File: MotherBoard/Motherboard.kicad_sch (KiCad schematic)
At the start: 31 parts, among them J1 22-28-4157, J2 X6521WV-2x15H-C60D30, Q1 NCE2302, SW1 FSM4JSMATR, SW2 FSM4JSMATR, U1 ESP32 S3, U2 Unidirectional 5.5V 6V SOT-14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, U4 LIS2MDLTR, U5 LIS3DHTR, U6 MAX7219M/TR, U7 C193852

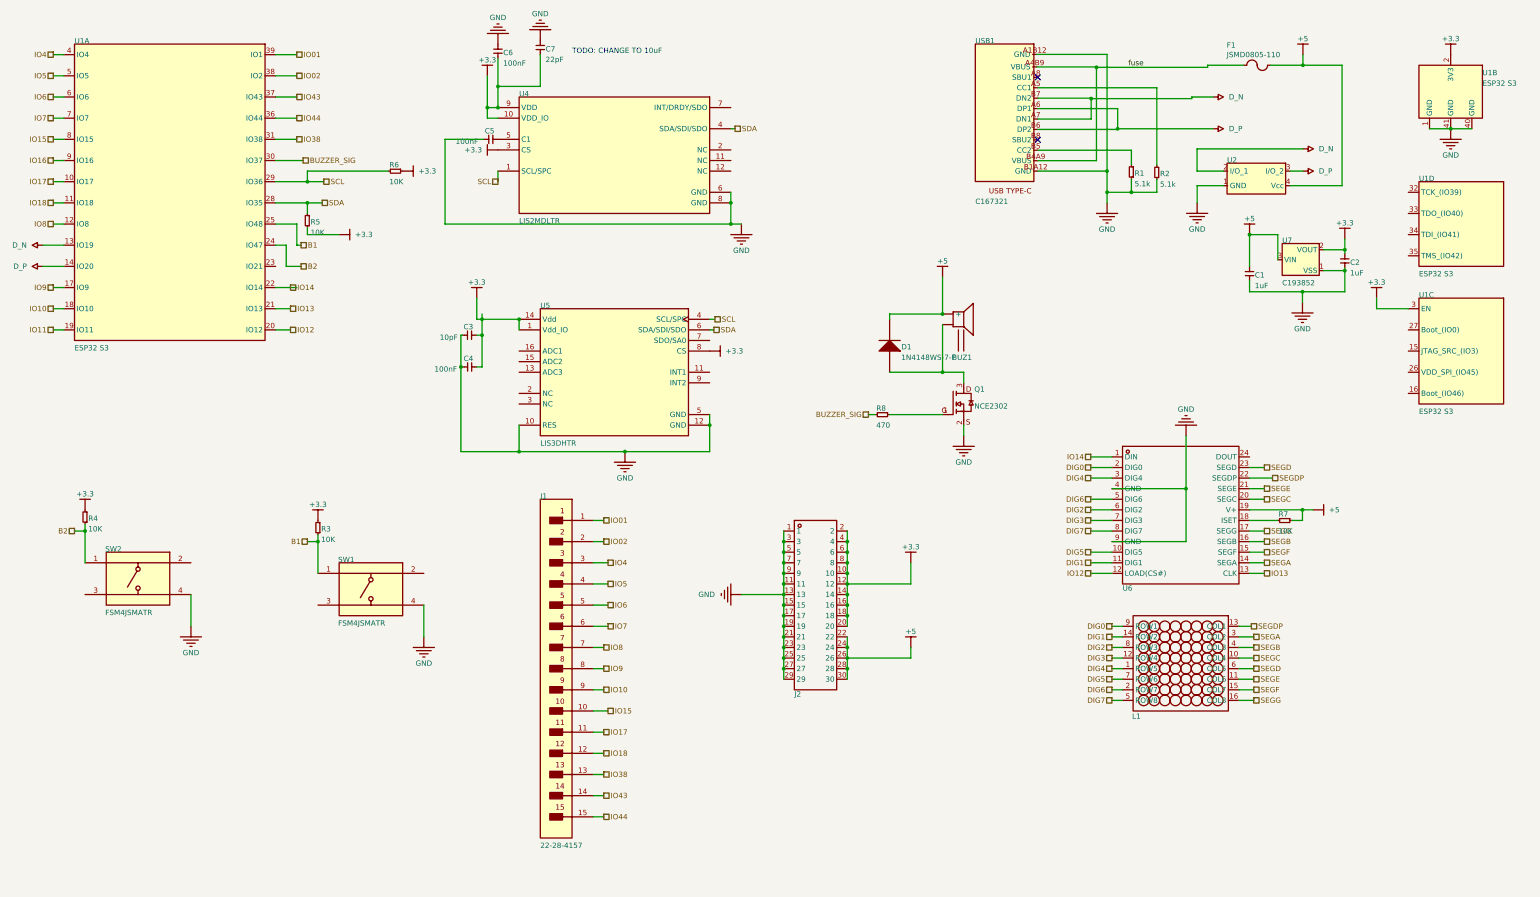
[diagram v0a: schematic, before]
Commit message: motherboard imported and corrected
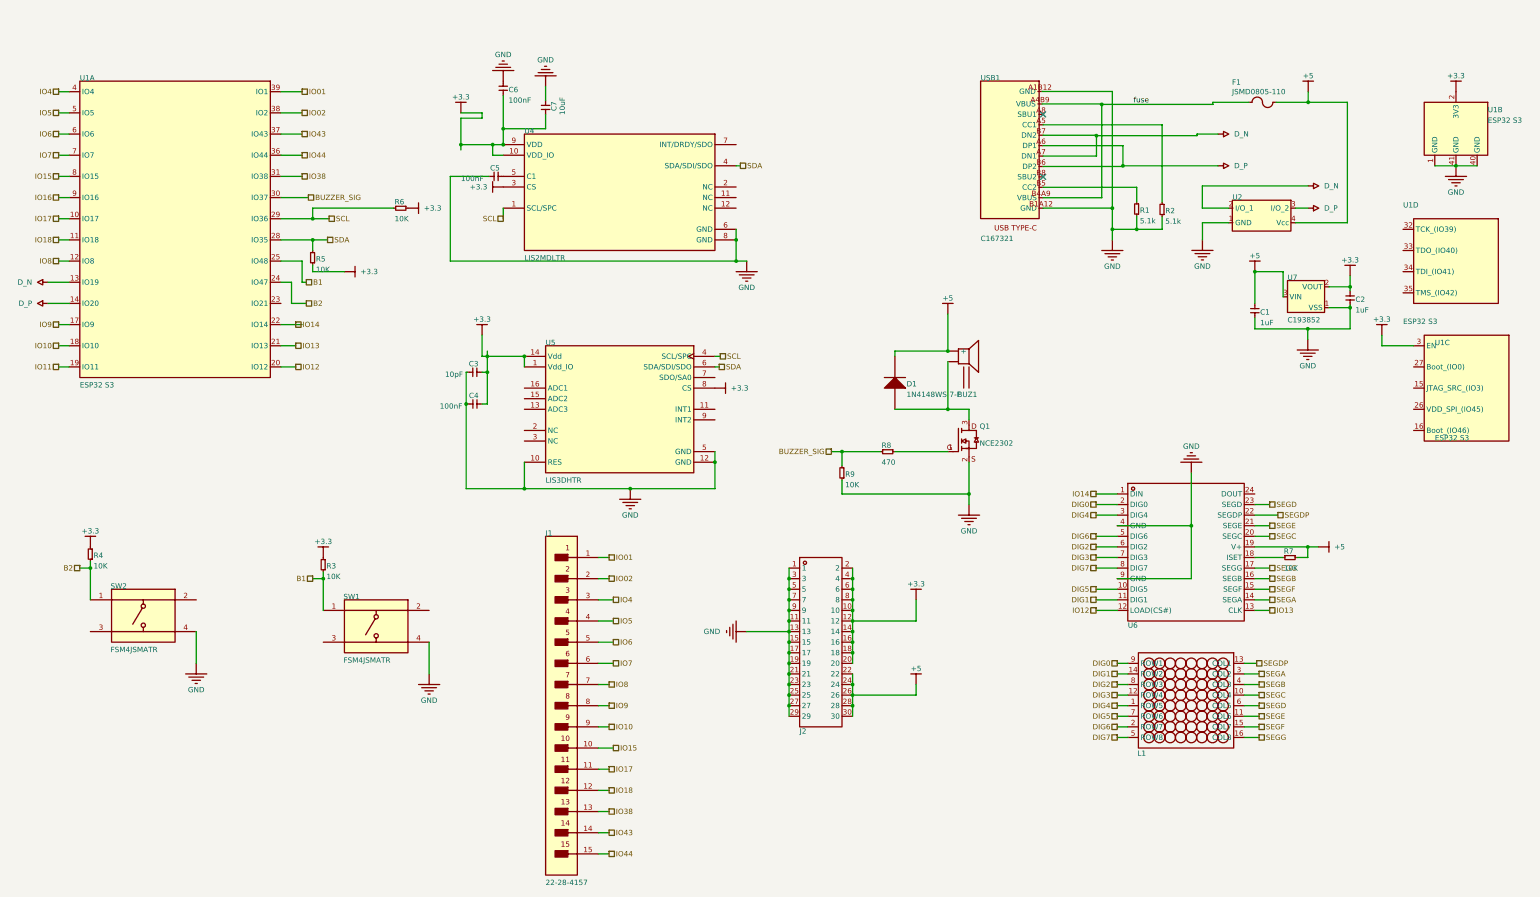
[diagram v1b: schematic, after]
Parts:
- removed C7: 22pF, 0402C, symbol Hub 2.0:root_1_TCC0402COG220K500AT_Hub 2.0.SchLib
- added C7: 10uF, FableFootPrintLibrary:0402C, symbol Hub 2.0:root_0_TCC0402COG100K500AT_Hub 2.0.SchLib
- added R9: 10K, FableFootPrintLibrary:0402R, symbol Hub 2.0:root_1_RC-02W103JT_Hub 2.0.SchLib
- BUZ1: footprint BUZ-SMD_4P-L8.5-W8.5-P8.50-BR -> FableFootPrintLibrary:BUZ-SMD_4P-L8.5-W8.5-P8.50-BR; SUPPLIER 1 (none) -> LCSC
- C1, C2: footprint 0402C -> FableFootPrintLibrary:0402C; SUPPLIER (none) -> LCSC; SUPPLIER PART (none) -> C60474; SUPPLIER PART NUMBER 1 C107372 -> C60474
- C3: footprint 0402C -> FableFootPrintLibrary:0402C; SUPPLIER (none) -> LCSC; SUPPLIER PART (none) -> C713505
- C4, C5, C6: footprint 0402C -> FableFootPrintLibrary:0402C; SUPPLIER (none) -> LCSC; SUPPLIER PART (none) -> C60474
- D1: footprint DIOD-SOD323-2-A_V -> FableFootPrintLibrary:DIOD-SOD323-2-A_V; SUPPLIER (none) -> LCSC; SUPPLIER PART (none) -> C60580
- F1: footprint 0805 -> FableFootPrintLibrary:0805; SUPPLIER (none) -> LCSC; SUPPLIER PART (none) -> C692712
- J1: footprint FP-22-28-4157-MFG -> FableFootPrintLibrary:FP-22-28-4157-MFG; SUPPLIER (none) -> LCSC; SUPPLIER PART (none) -> C725887
- J2: footprint HDR-TH_30P-P2.54-V-M-R2-C15-S2.54-BL -> FableFootPrintLibrary:HDR-TH_30P-P2.54-V-F-R2-C15-S2.54; SUPPLIER 1 (none) -> LCSC
- L1: footprint LED-SEG-TH_SZ421288N-64 -> FableFootPrintLibrary:LED-SEG-TH_SZ421288N-64; SUPPLIER 1 (none) -> LCSC
- Q1: footprint FableFootPrintLibrary.PcbLib:SOT-23 -> FableFootPrintLibrary:SOT-23; SUPPLIER (none) -> LCSC; SUPPLIER PART (none) -> C132123
- R1, R2: footprint FableFootPrintLibrary.PcbLib:0402R -> FableFootPrintLibrary:0402R; SUPPLIER (none) -> LCSC; SUPPLIER PART (none) -> C258132
- R3, R4, R5, R6, R7: footprint 0402R -> FableFootPrintLibrary:0402R; SUPPLIER (none) -> LCSC; SUPPLIER PART (none) -> C140214
- R8: footprint 0402R -> FableFootPrintLibrary:0402R; SUPPLIER (none) -> LCSC; SUPPLIER PART (none) -> C208991
- SW1, SW2: footprint TECO-FSM4JSMATR_V -> FableFootPrintLibrary:TECO-FSM4JSMATR_V; DATASHEET (none) -> https://www.lcsc.com/datasheet/C2680629.pdf; SUPPLIER (none) -> LCSC; SUPPLIER PART (none) -> C2680629
- U1: footprint FableFootPrintLibrary.PcbLib:ESP32 S3 WROOM 1 -> FableFootPrintLibrary:ESP32 S3 WROOM 1; DATASHEET (none) -> https://www.lcsc.com/datasheet/C2913202.pdf; SUPPLIER (none) -> LCSC; SUPPLIER PART (none) -> C2913202
- U2: footprint SOT143B -> FableFootPrintLibrary:SOT143B; SUPPLIER (none) -> LCSC; SUPPLIER PART (none) -> C12333
- U4: footprint FP-LGA-12-DM00170568-MFG -> FableFootPrintLibrary:FP-LGA-12-DM00170568-MFG; DATASHEET (none) -> https://www.lcsc.com/datasheet/C919695.pdf; SUPPLIER (none) -> LCSC; SUPPLIER PART (none) -> C919695
- U5: footprint FP-LGA-16-7983231-MFG -> FableFootPrintLibrary:FP-LGA-16-7983231-MFG; DATASHEET (none) -> https://www.lcsc.com/datasheet/C15134.pdf; SUPPLIER (none) -> LCSC; SUPPLIER 1 (none) -> LCSC; SUPPLIER PART (none) -> C15134
- U6: footprint SOP-24_L15.4-W7.5-P1.27-LS10.4-BL -> FableFootPrintLibrary:SOP-24_L15.4-W7.5-P1.27-LS10.4-BL; SUPPLIER 1 (none) -> LCSC
- U7: footprint SOT-23 -> FableFootPrintLibrary:SOT-23; SUPPLIER (none) -> LCSC; SUPPLIER PART (none) -> C193852
- USB1: footprint C167321 -> FableFootPrintLibrary:C167321; SUPPLIER (none) -> LCSC; SUPPLIER PART (none) -> C167321
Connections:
- net +3.3: now also U1.3 (EN), C7.2; no longer U1.3 (EN)
- net BUZZER_SIG: now also R9.2
- net GND: now also C7.1, R9.1
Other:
- note removed: "TODO: CHANGE TO 10uF"
- moved on the sheet: BUZ1, C1, C2, C3, C4, C5, C6, D1, F1, J1, J2, L1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
